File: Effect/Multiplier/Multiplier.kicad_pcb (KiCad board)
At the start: 2 copper layers, 32 x 68.5 mm, 49 parts, among them J1 Conn_01x04_Pin, J2 Conn_01x03_Pin, U1 OPA1656, U2 OPA1656, U3 OPA1656, U4 OPA1656

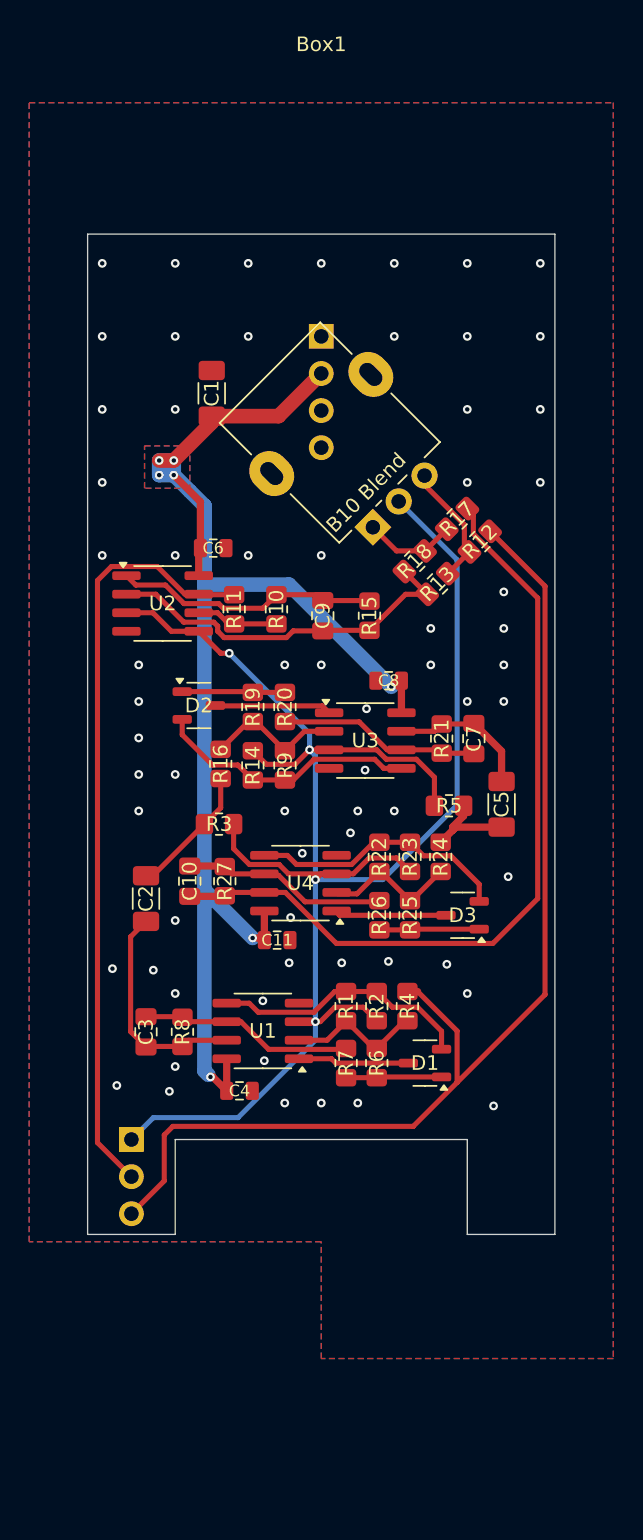
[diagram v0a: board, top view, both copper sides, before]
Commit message: Turn the multiplier schematic into a testable board
This is a very random effect, but might as well test it out to see if
the simulation matches any kind of reality.

Signed-off-by: Linus Torvalds <torvalds@linux-foundation.org>
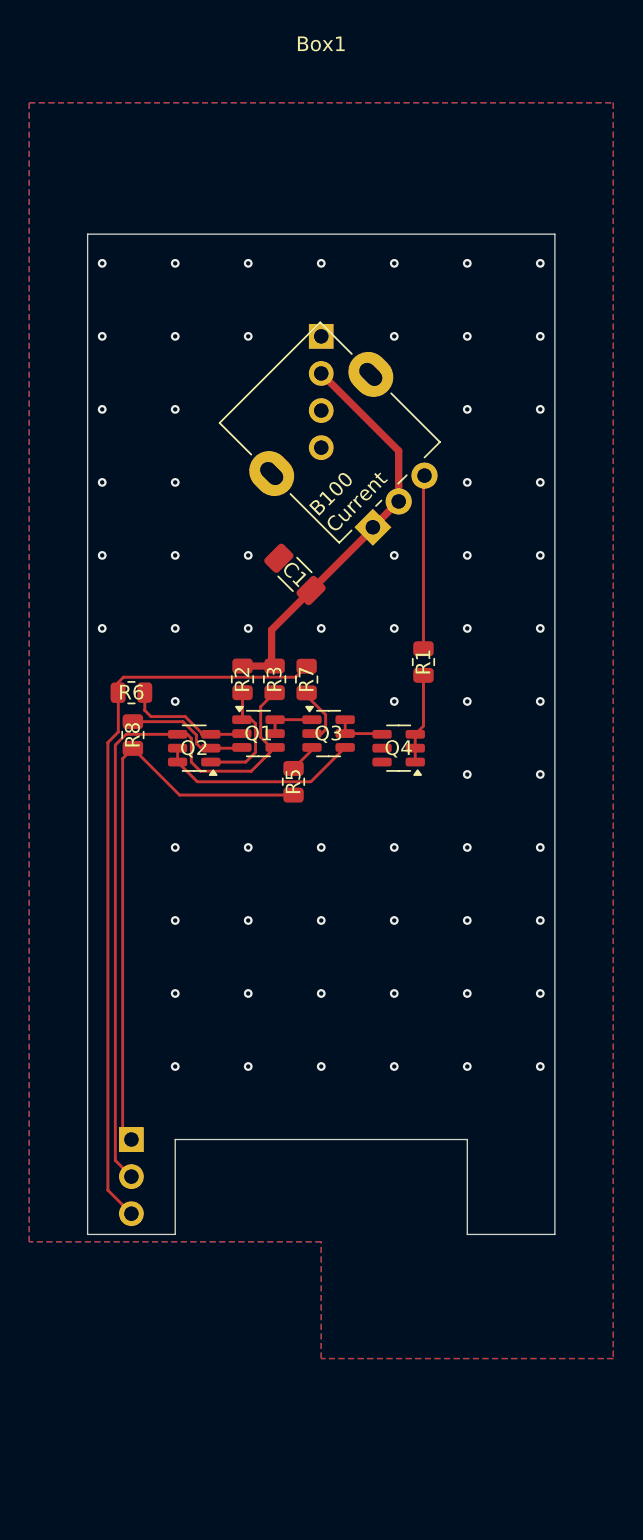
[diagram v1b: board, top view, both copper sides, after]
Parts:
- removed C10, C3, C7, C9: 47pF, Capacitor_SMD:C_0805_2012Metric_Pad1.18x1.45mm_HandSolder
- removed C11, C4, C6, C8: 0.1uF, Mylib:C_0704_1810Metric
- removed C2, C5: 0.47uF, Capacitor_SMD:C_1206_3216Metric_Pad1.33x1.80mm_HandSolder
- removed D1, D2, D3: BAT54S, Package_TO_SOT_SMD:SOT-23-3
- removed R10, R11, R19, R20, R21, R22, R25, R26, R27, R9: 10k, Resistor_SMD:R_0805_2012Metric_Pad1.20x1.40mm_HandSolder
- removed R12, R13, R17, R18: 15k, Resistor_SMD:R_0805_2012Metric_Pad1.20x1.40mm_HandSolder
- removed R14, R23: 2k, Resistor_SMD:R_0805_2012Metric_Pad1.20x1.40mm_HandSolder
- removed R15: 51k, Resistor_SMD:R_0805_2012Metric_Pad1.20x1.40mm_HandSolder
- removed R16, R24: 6.8k, Resistor_SMD:R_0805_2012Metric_Pad1.20x1.40mm_HandSolder
- removed R4: 2.7k, Resistor_SMD:R_0805_2012Metric_Pad1.20x1.40mm_HandSolder
- removed U1, U2, U3, U4: OPA1656, Package_SO:SOIC-8_3.9x4.9mm_P1.27mm
- added Q1: DMMT5551, Package_TO_SOT_SMD:SOT-23-6, F.Cu at (95.7, 97.2)
- added Q2: DMMT5551, Package_TO_SOT_SMD:SOT-23-6, F.Cu at (91.3, 98.2)
- added Q3: DMMT5551, Package_TO_SOT_SMD:SOT-23-6, F.Cu at (100.5, 97.2)
- added Q4: DMMT5551, Package_TO_SOT_SMD:SOT-23-6, F.Cu at (105.3, 98.2)
- R1: footprint Resistor_SMD:R_0805_2012Metric_Pad1.20x1.40mm_HandSolder -> Resistor_SMD:R_0805_2012Metric
- R2: value 2k -> 10k; footprint Resistor_SMD:R_0805_2012Metric_Pad1.20x1.40mm_HandSolder -> Resistor_SMD:R_0805_2012Metric
- R3: value 100k -> 10k; footprint Resistor_SMD:R_0805_2012Metric_Pad1.20x1.40mm_HandSolder -> Resistor_SMD:R_0805_2012Metric
- R5: value 100k -> 22k; footprint Resistor_SMD:R_0805_2012Metric_Pad1.20x1.40mm_HandSolder -> Resistor_SMD:R_0805_2012Metric
- R6, R7, R8: value 10k -> 22k; footprint Resistor_SMD:R_0805_2012Metric_Pad1.20x1.40mm_HandSolder -> Resistor_SMD:R_0805_2012Metric
- RV1: value B10k Blend -> Current
- moved R6 30.4 mm to (87.0, 94.4), turned to 0 degrees
- moved R7 26.4 mm to (99.0, 93.5), turned to -90 degrees
- moved R2 24.2 mm to (94.6, 93.5), turned to -90 degrees
- moved R1 24.2 mm to (107.0, 92.3), turned to -90 degrees
- moved R8 20.6 mm to (87.1, 97.3), turned to 90 degrees
- moved C1 13.6 mm to (98.2, 86.3), turned to 135 degrees
- moved R5 10.8 mm to (98.1, 100.5), turned to 90 degrees
- moved R3 10.6 mm to (96.8, 93.5), turned to -90 degrees
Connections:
- J2 pad 3: IN1 -> IN
- R1 pad 1: Net-(U1A--) -> Net-(R1-Pad1)
- R1 pad 2: Net-(U1B-+) -> Net-(Q4A-B)
- R2 pad 1: GNDREF -> +V
- R2 pad 2: Net-(U1B-+) -> Net-(Q1A-C)
- R3 pad 1: GNDREF -> +V
- R3 pad 2: IN2 -> OUT
- R5 pad 2: IN3 -> Net-(Q3B-B)
- R6 pad 1: Net-(U1A--) -> IN
- R6 pad 2: Net-(D1A-A) -> Net-(Q1A-B)
- R7 pad 1: Net-(D1A-A) -> IN
- R7 pad 2: Net-(U1B--) -> Net-(Q3A-B)
- R8 pad 1: Net-(U1B--) -> GNDREF
- R8 pad 2: OUT1 -> Net-(Q1B-B)
- RV1 pad 1: Net-(R17-Pad1) -> +V
- RV1 pad 2: GNDREF -> +V
- RV1 pad 3: Net-(R12-Pad1) -> Net-(R1-Pad1)
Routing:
- net GNDREF: track 125.9 -> 39.7 mm, vias 4 -> 0
- net IN1: track 77.7 -> 0.00 mm
- net +V: track 102.6 -> 28.2 mm, vias 7 -> 0
- net OUT3: track 55.0 -> 0.00 mm
- net IN: track 0.00 -> 50.9 mm
- net Net-(U2A--): track 25.4 -> 0.00 mm
- net Net-(U3B-+): track 18.2 -> 0.00 mm
- net Net-(U1B-+): track 17.9 -> 0.00 mm
- net Net-(U4B-+): track 17.6 -> 0.00 mm
- net Net-(U2A-OUT): track 17.5 -> 0.00 mm
- net OUT1: track 14.5 -> 0.00 mm
- net Net-(U1B--): track 14.1 -> 0.00 mm
- net Net-(Q2A-E): track 0.00 -> 14.0 mm
- net Net-(U4B--): track 13.7 -> 0.00 mm
- net Net-(U3B--): track 13.4 -> 0.00 mm
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- removed copper zone on B.Cu, net +V
- removed copper zone on F.Cu, net +V
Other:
- board text added: "B100 Current"
- board text removed: "B10 Blend"
